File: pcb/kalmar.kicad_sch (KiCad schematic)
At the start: 21 parts, among them J1 MJ-4PP-9, SW1 SW_SPDT, U1 ProMicro_r

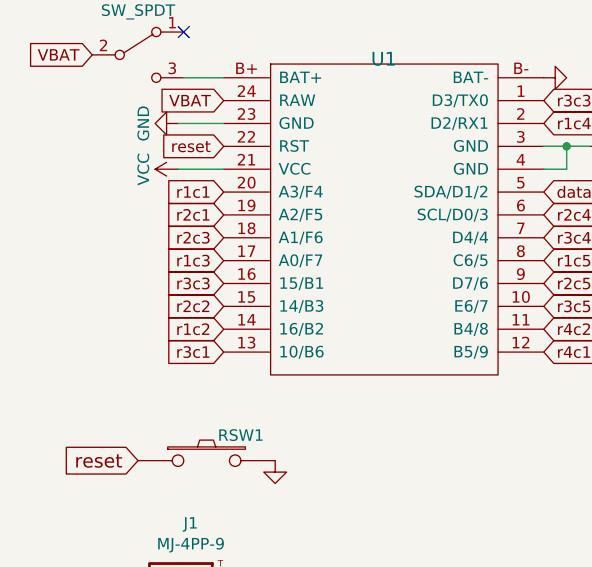
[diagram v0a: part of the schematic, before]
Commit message: v0.3
fix connection
add jack cut
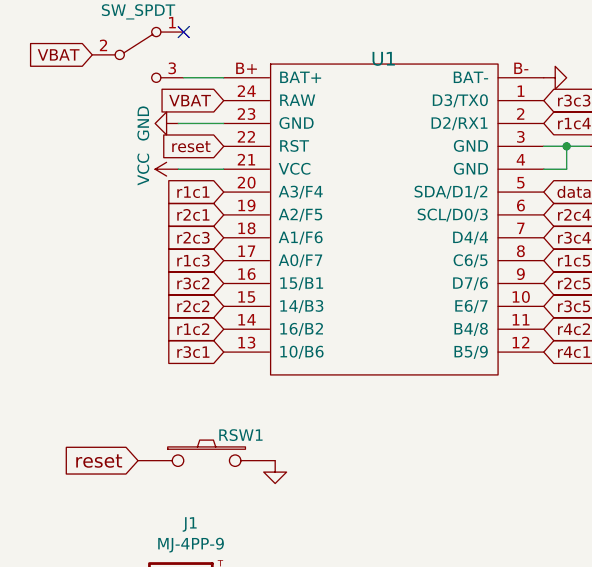
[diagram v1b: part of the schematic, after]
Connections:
- net r3c2: now also U1.16 (15/B1)
- net r3c3: no longer U1.16 (15/B1)
